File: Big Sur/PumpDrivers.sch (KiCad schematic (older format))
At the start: 3 parts, among them Q1 TSM900N10

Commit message: Work on pump drivers.
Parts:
- added D?: NTS12120EMFST1G, symbol Device:D_Schottky
- added Q?: TSM900N10, symbol Device:Q_NMOS_GDS
- added R?: 100K, symbol Device:R_US
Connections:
- net +24V: now also D?.1 (K)
- net GND: now also Q?.3 (S), R?.2
- new net PUMP_INPUT_2: Q?.1 (G), R?.1
- new net PUMP_LS_CHANNEL_2: D?.2 (A), Q?.2 (D)
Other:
- note removed: "Designing these to be low-side drivers cause why n-\nwait, why aren't we just using motor driver ICs for pumps\nlike we are for solenoids? They have safety features.\nAnd serial control. And blackjack. And hookers.\nOkay maybe not all of those, but still."
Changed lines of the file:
@@
 	1    0    0    -1
 $EndComp
-Text Notes 2650 2450 0    50   ~ 0
-Designing these to be low-side drivers cause why n-\nwait, why aren't we just using motor driver ICs for pumps\nlike we are for solenoids? They have safety features.\nAnd serial control. And blackjack. And hookers.\nOkay maybe not all of those, but still.
 Wire Wire Line
 	2500 1700 2500 1600
@@
 Text GLabel 1700 1900 0    50   BiDi ~ 0
 PUMP_INPUT_1
+$Comp
+L Device:Q_NMOS_GDS Q?
+U 1 1 5D85B099
+P 2400 3700
+F 0 "Q?" H 2606 3746 50  0000 L CNN
+F 1 "TSM900N10" H 2606 3655 50  0000 L CNN
+F 2 "" H 2600 3800 50  0001 C CNN
+F 3 "https://www.taiwansemi.com/products/datasheet/TSM900N10_A15.pdf" H 2400 3700 50  0001 C CNN
+F 4 "https://www.digikey.ca/product-detail/en/taiwan-semiconductor-corporation/TSM900N10CP-ROG/TSM900N10CPROGCT-ND/7360607" H 2400 3700 50  0001 C CNN "Digikey"
+	1    2400 3700
+	1    0    0    -1
+$EndComp
+Wire Wire Line
+	2500 3900 2500 4150
+$Comp
+L power:GND #PWR?
+U 1 1 5D85B0A4
+P 2500 4150
+F 0 "#PWR?" H 2500 3900 50  0001 C CNN
+F 1 "GND" H 2505 3977 50  0000 C CNN
+F 2 "" H 2500 4150 50  0001 C CNN
+F 3 "" H 2500 4150 50  0001 C CNN
+	1    2500 4150
+	1    0    0    -1
+$EndComp
+Wire Wire Line
+	2500 3500 2500 3400
+Wire Wire Line
+	2500 3400 2650 3400
+Text GLabel 2650 3400 2    50   BiDi ~ 0
+PUMP_LS_CHANNEL_2
+Connection ~ 2500 3400
+Wire Wire Line
+	2200 3700 2000 3700
+Wire Wire Line
+	2000 3700 2000 3750
+Connection ~ 2000 3700
+Wire Wire Line
+	2000 3700 1700 3700
+$Comp
+L Device:R_US R?
+U 1 1 5D85B0B6
+P 2000 3900
+F 0 "R?" H 2068 3946 50  0000 L CNN
+F 1 "100K" H 2068 3855 50  0000 L CNN
+F 2 "" V 2040 3890 50  0001 C CNN
+F 3 "~" H 2000 3900 50  0001 C CNN
+	1    2000 3900
+	1    0    0    -1
+$EndComp
+$Comp
+L power:GND #PWR?
+U 1 1 5D85B0C0
+P 2000 4150
+F 0 "#PWR?" H 2000 3900 50  0001 C CNN
+F 1 "GND" H 2005 3977 50  0000 C CNN
+F 2 "" H 2000 4150 50  0001 C CNN
+F 3 "" H 2000 4150 50  0001 C CNN
+	1    2000 4150
+	1    0    0    -1
+$EndComp
+Wire Wire Line
+	2000 4150 2000 4050
+Wire Wire Line
+	2500 3350 2500 3400
+$Comp
+L power:+24V #PWR?
+U 1 1 5D85B0CC
+P 2500 2950
+F 0 "#PWR?" H 2500 2800 50  0001 C CNN
+F 1 "+24V" H 2515 3123 50  0000 C CNN
+F 2 "" H 2500 2950 50  0001 C CNN
+F 3 "" H 2500 2950 50  0001 C CNN
+	1    2500 2950
+	1    0    0    -1
+$EndComp
+$Comp
+L Device:D_Schottky D?
+U 1 1 5D85B0D7
+P 2500 3200
+F 0 "D?" V 2454 3279 50  0000 L CNN
+F 1 "NTS12120EMFST1G" V 2545 3279 50  0000 L CNN
+F 2 "" H 2500 3200 50  0001 C CNN
+F 3 "https://www.onsemi.com/pub/Collateral/NTS12120EMFS-D.PDF" H 2500 3200 50  0001 C CNN
+F 4 "https://www.digikey.ca/product-detail/en/on-semiconductor/NTS12120EMFST1G/NTS12120EMFST1GOSCT-ND/8538813" V 2500 3200 50  0001 C CNN "Digikey"
+	1    2500 3200
+	0    1    1    0
+$EndComp
+Wire Wire Line
+	2500 2950 2500 3050
+Text GLabel 1700 3700 0    50   BiDi ~ 0
+PUMP_INPUT_2
 $EndSCHEMATC

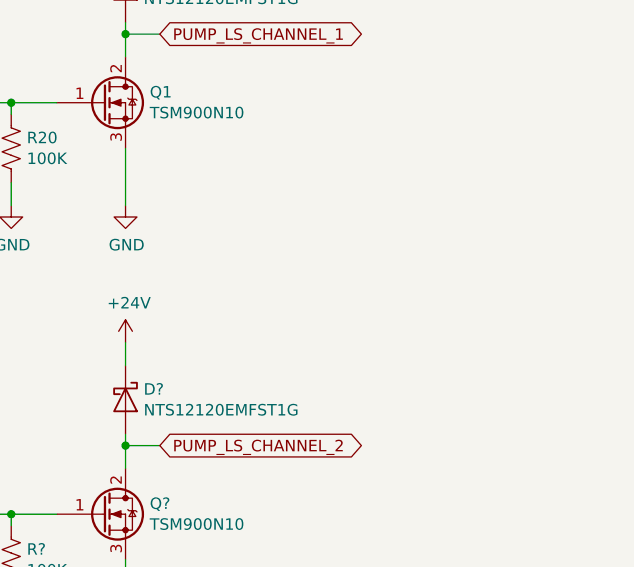
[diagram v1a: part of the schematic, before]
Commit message: Started filling in pinout of Paraduino connector, based on current Paraduino schematic.
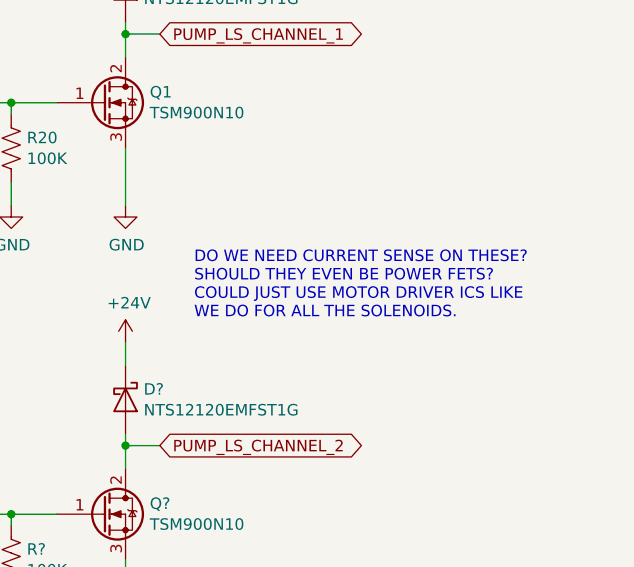
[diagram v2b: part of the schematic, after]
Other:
- note added: "DO WE NEED CURRENT SENSE ON THESE?\nSHOULD THEY EVEN BE POWER FETS?\nCOULD JUST USE MOTOR DRIVER ICS LIKE\nWE DO FOR ALL THE SOLENOIDS."
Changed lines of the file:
@@
 Text GLabel 1700 3700 0    50   BiDi ~ 0
 PUMP_INPUT_2
+Text Notes 2800 2850 0    50   ~ 0
+DO WE NEED CURRENT SENSE ON THESE?\nSHOULD THEY EVEN BE POWER FETS?\nCOULD JUST USE MOTOR DRIVER ICS LIKE\nWE DO FOR ALL THE SOLENOIDS.
 $EndSCHEMATC

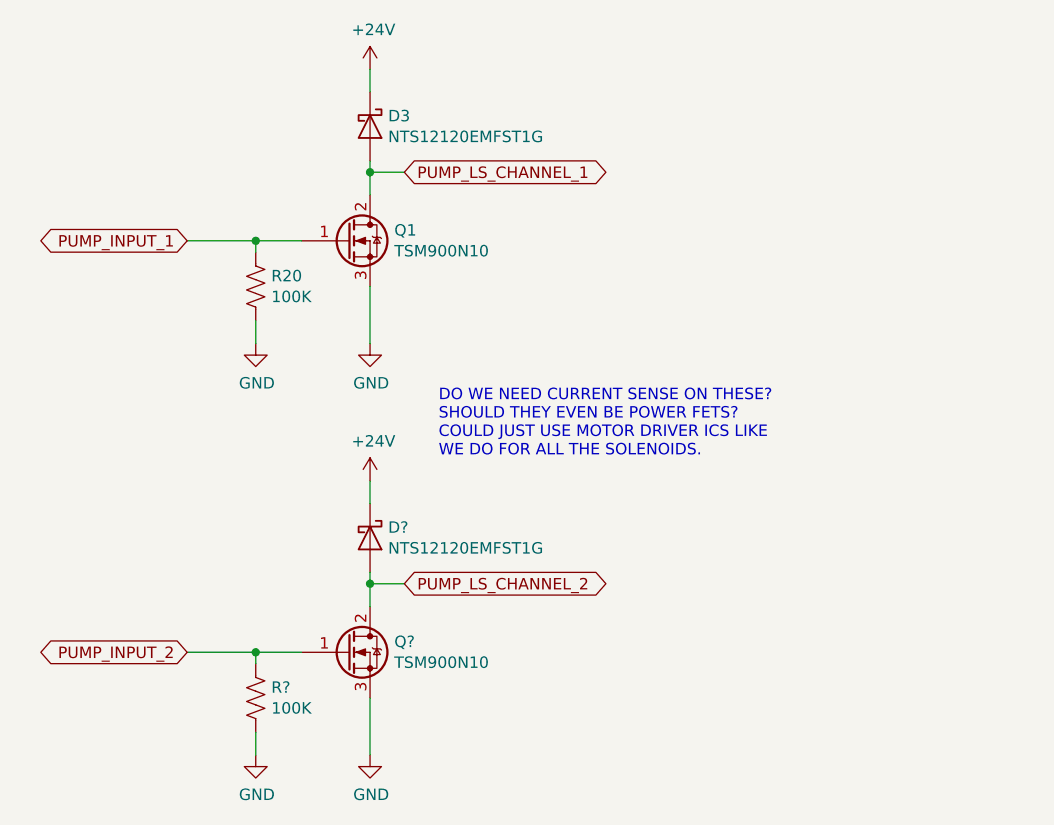
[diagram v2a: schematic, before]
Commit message: Updated current sense, second pump driver, solenoid connectors
-Current sense now uses current sense ICs, connected to Paraduino ADC pins.
-Added second pump driver.
-Connected outputs with XT30 connectors.
-Still need some Paraduino connections, inverter driver, footprints.
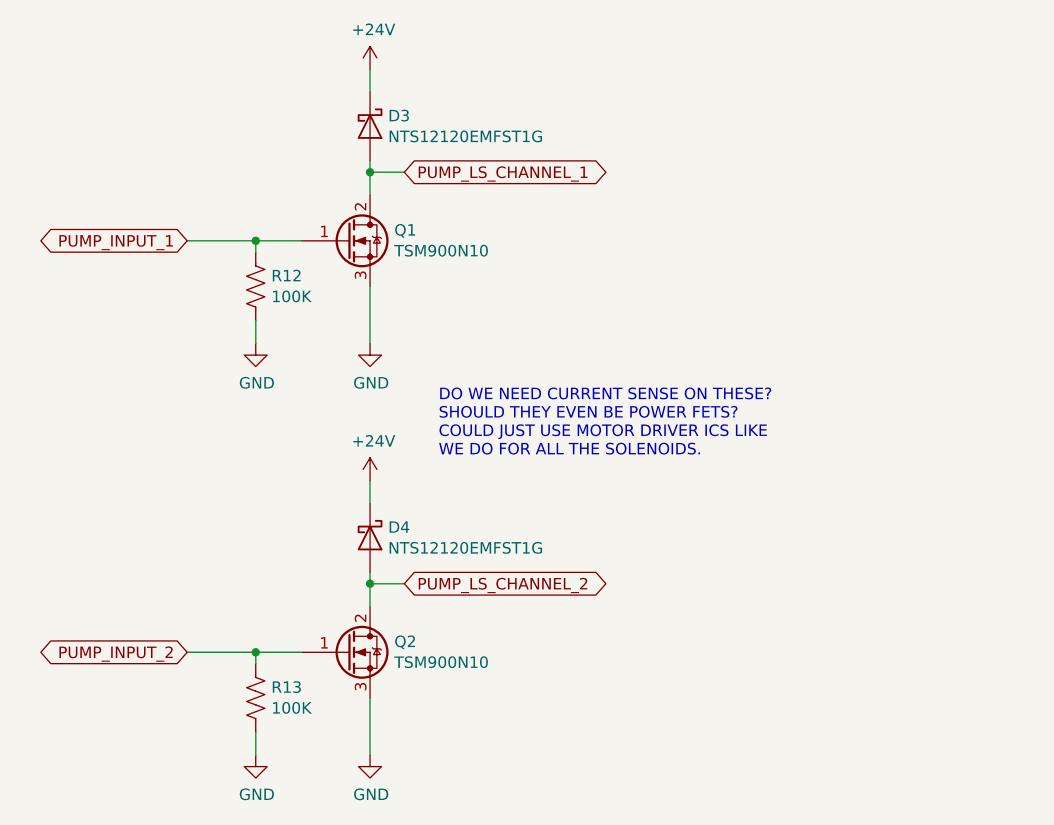
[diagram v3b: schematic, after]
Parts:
- gave numbers to parts that had none: 3
- renumbered R20 to R12
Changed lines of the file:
@@
 	2500 2100 2500 2350
 $Comp
-L power:GND #PWR033
+L power:GND #PWR038
 U 1 1 5D7D4C28
 P 2500 2350
-F 0 "#PWR033" H 2500 2100 50  0001 C CNN
+F 0 "#PWR038" H 2500 2100 50  0001 C CNN
 F 1 "GND" H 2505 2177 50  0000 C CNN
 F 2 "" H 2500 2350 50  0001 C CNN
@@
 	2000 1900 1700 1900
 $Comp
-L Device:R_US R20
+L Device:R_US R12
 U 1 1 5D7D75FE
 P 2000 2100
-F 0 "R20" H 2068 2146 50  0000 L CNN
+F 0 "R12" H 2068 2146 50  0000 L CNN
 F 1 "100K" H 2068 2055 50  0000 L CNN
 F 2 "" V 2040 2090 50  0001 C CNN
@@
 $EndComp
 $Comp
-L power:GND #PWR032
+L power:GND #PWR037
 U 1 1 5D7D85EE
 P 2000 2350
-F 0 "#PWR032" H 2000 2100 50  0001 C CNN
+F 0 "#PWR037" H 2000 2100 50  0001 C CNN
 F 1 "GND" H 2005 2177 50  0000 C CNN
 F 2 "" H 2000 2350 50  0001 C CNN
@@
 	2500 1550 2500 1600
 $Comp
-L power:+24V #PWR031
+L power:+24V #PWR036
 U 1 1 5D6DC51E
 P 2500 1150
-F 0 "#PWR031" H 2500 1000 50  0001 C CNN
+F 0 "#PWR036" H 2500 1000 50  0001 C CNN
 F 1 "+24V" H 2515 1323 50  0000 C CNN
 F 2 "" H 2500 1150 50  0001 C CNN
@@
 PUMP_INPUT_1
 $Comp
-L Device:Q_NMOS_GDS Q?
+L Device:Q_NMOS_GDS Q2
 U 1 1 5D85B099
 P 2400 3700
-F 0 "Q?" H 2606 3746 50  0000 L CNN
+F 0 "Q2" H 2606 3746 50  0000 L CNN
 F 1 "TSM900N10" H 2606 3655 50  0000 L CNN
 F 2 "" H 2600 3800 50  0001 C CNN
@@
 	2500 3900 2500 4150
 $Comp
-L power:GND #PWR?
+L power:GND #PWR041
 U 1 1 5D85B0A4
 P 2500 4150
-F 0 "#PWR?" H 2500 3900 50  0001 C CNN
+F 0 "#PWR041" H 2500 3900 50  0001 C CNN
 F 1 "GND" H 2505 3977 50  0000 C CNN
 F 2 "" H 2500 4150 50  0001 C CNN
@@
 	2000 3700 1700 3700
 $Comp
-L Device:R_US R?
+L Device:R_US R13
 U 1 1 5D85B0B6
 P 2000 3900
-F 0 "R?" H 2068 3946 50  0000 L CNN
+F 0 "R13" H 2068 3946 50  0000 L CNN
 F 1 "100K" H 2068 3855 50  0000 L CNN
 F 2 "" V 2040 3890 50  0001 C CNN
@@
 $EndComp
 $Comp
-L power:GND #PWR?
+L power:GND #PWR040
 U 1 1 5D85B0C0
 P 2000 4150
-F 0 "#PWR?" H 2000 3900 50  0001 C CNN
+F 0 "#PWR040" H 2000 3900 50  0001 C CNN
 F 1 "GND" H 2005 3977 50  0000 C CNN
 F 2 "" H 2000 4150 50  0001 C CNN
@@
 	2500 3350 2500 3400
 $Comp
-L power:+24V #PWR?
+L power:+24V #PWR039
 U 1 1 5D85B0CC
 P 2500 2950
-F 0 "#PWR?" H 2500 2800 50  0001 C CNN
+F 0 "#PWR039" H 2500 2800 50  0001 C CNN
 F 1 "+24V" H 2515 3123 50  0000 C CNN
 F 2 "" H 2500 2950 50  0001 C CNN
@@
 $EndComp
 $Comp
-L Device:D_Schottky D?
+L Device:D_Schottky D4
 U 1 1 5D85B0D7
 P 2500 3200
-F 0 "D?" V 2454 3279 50  0000 L CNN
+F 0 "D4" V 2454 3279 50  0000 L CNN
 F 1 "NTS12120EMFST1G" V 2545 3279 50  0000 L CNN
 F 2 "" H 2500 3200 50  0001 C CNN

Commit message: Removed Inverter
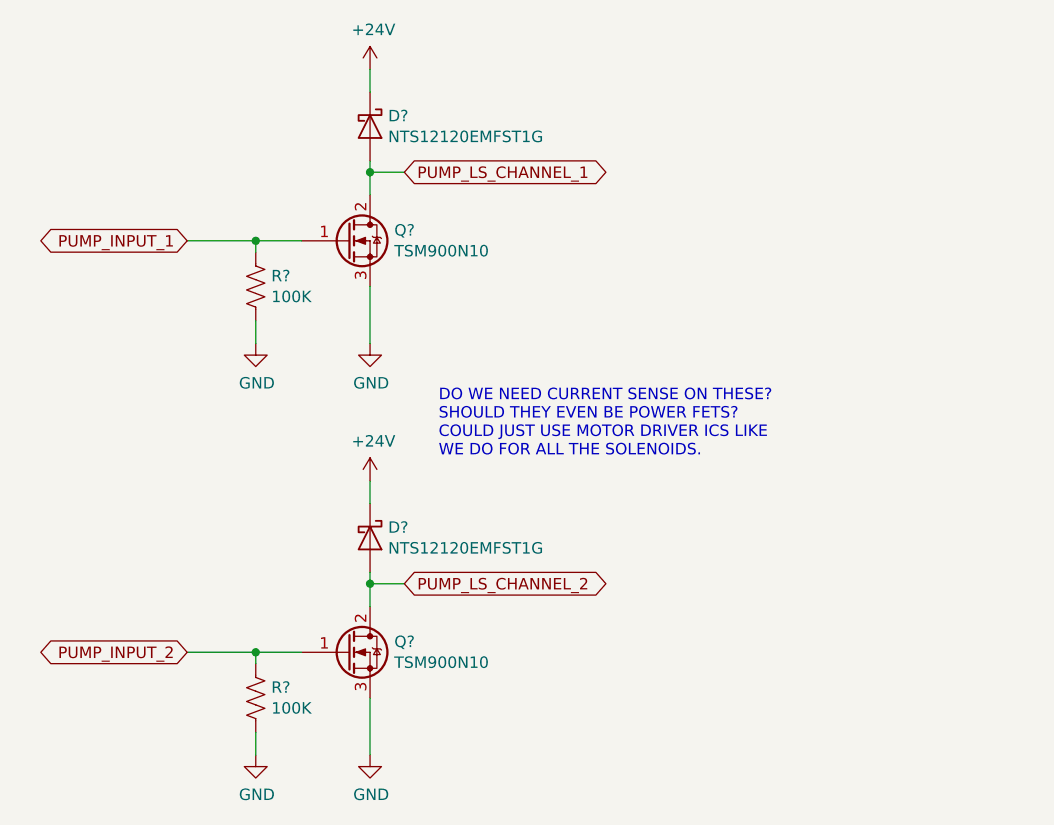
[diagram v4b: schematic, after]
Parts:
- renumbered D3 to D?, D4 to D?, Q1 to Q?, Q2 to Q?, R12 to R?, R13 to R?
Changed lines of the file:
@@
 $EndDescr
 $Comp
-L Device:Q_NMOS_GDS Q1
+L Device:Q_NMOS_GDS Q?
 U 1 1 5D7D3E10
 P 2400 1900
-F 0 "Q1" H 2606 1946 50  0000 L CNN
+F 0 "Q?" H 2606 1946 50  0000 L CNN
 F 1 "TSM900N10" H 2606 1855 50  0000 L CNN
 F 2 "" H 2600 2000 50  0001 C CNN
@@
 	2500 2100 2500 2350
 $Comp
-L power:GND #PWR038
+L power:GND #PWR?
 U 1 1 5D7D4C28
 P 2500 2350
-F 0 "#PWR038" H 2500 2100 50  0001 C CNN
+F 0 "#PWR?" H 2500 2100 50  0001 C CNN
 F 1 "GND" H 2505 2177 50  0000 C CNN
 F 2 "" H 2500 2350 50  0001 C CNN
@@
 	2000 1900 1700 1900
 $Comp
-L Device:R_US R12
+L Device:R_US R?
 U 1 1 5D7D75FE
 P 2000 2100
-F 0 "R12" H 2068 2146 50  0000 L CNN
+F 0 "R?" H 2068 2146 50  0000 L CNN
 F 1 "100K" H 2068 2055 50  0000 L CNN
 F 2 "" V 2040 2090 50  0001 C CNN
@@
 $EndComp
 $Comp
-L power:GND #PWR037
+L power:GND #PWR?
 U 1 1 5D7D85EE
 P 2000 2350
-F 0 "#PWR037" H 2000 2100 50  0001 C CNN
+F 0 "#PWR?" H 2000 2100 50  0001 C CNN
 F 1 "GND" H 2005 2177 50  0000 C CNN
 F 2 "" H 2000 2350 50  0001 C CNN
@@
 	2500 1550 2500 1600
 $Comp
-L power:+24V #PWR036
+L power:+24V #PWR?
 U 1 1 5D6DC51E
 P 2500 1150
-F 0 "#PWR036" H 2500 1000 50  0001 C CNN
+F 0 "#PWR?" H 2500 1000 50  0001 C CNN
 F 1 "+24V" H 2515 1323 50  0000 C CNN
 F 2 "" H 2500 1150 50  0001 C CNN
@@
 $EndComp
 $Comp
-L Device:D_Schottky D3
+L Device:D_Schottky D?
 U 1 1 5D6DD7E1
 P 2500 1400
-F 0 "D3" V 2454 1479 50  0000 L CNN
+F 0 "D?" V 2454 1479 50  0000 L CNN
 F 1 "NTS12120EMFST1G" V 2545 1479 50  0000 L CNN
 F 2 "" H 2500 1400 50  0001 C CNN
@@
 PUMP_INPUT_1
 $Comp
-L Device:Q_NMOS_GDS Q2
+L Device:Q_NMOS_GDS Q?
 U 1 1 5D85B099
 P 2400 3700
-F 0 "Q2" H 2606 3746 50  0000 L CNN
+F 0 "Q?" H 2606 3746 50  0000 L CNN
 F 1 "TSM900N10" H 2606 3655 50  0000 L CNN
 F 2 "" H 2600 3800 50  0001 C CNN
@@
 	2500 3900 2500 4150
 $Comp
-L power:GND #PWR041
+L power:GND #PWR?
 U 1 1 5D85B0A4
 P 2500 4150
-F 0 "#PWR041" H 2500 3900 50  0001 C CNN
+F 0 "#PWR?" H 2500 3900 50  0001 C CNN
 F 1 "GND" H 2505 3977 50  0000 C CNN
 F 2 "" H 2500 4150 50  0001 C CNN
@@
 	2000 3700 1700 3700
 $Comp
-L Device:R_US R13
+L Device:R_US R?
 U 1 1 5D85B0B6
 P 2000 3900
-F 0 "R13" H 2068 3946 50  0000 L CNN
+F 0 "R?" H 2068 3946 50  0000 L CNN
 F 1 "100K" H 2068 3855 50  0000 L CNN
 F 2 "" V 2040 3890 50  0001 C CNN
@@
 $EndComp
 $Comp
-L power:GND #PWR040
+L power:GND #PWR?
 U 1 1 5D85B0C0
 P 2000 4150
-F 0 "#PWR040" H 2000 3900 50  0001 C CNN
+F 0 "#PWR?" H 2000 3900 50  0001 C CNN
 F 1 "GND" H 2005 3977 50  0000 C CNN
 F 2 "" H 2000 4150 50  0001 C CNN
@@
 	2500 3350 2500 3400
 $Comp
-L power:+24V #PWR039
+L power:+24V #PWR?
 U 1 1 5D85B0CC
 P 2500 2950
-F 0 "#PWR039" H 2500 2800 50  0001 C CNN
+F 0 "#PWR?" H 2500 2800 50  0001 C CNN
 F 1 "+24V" H 2515 3123 50  0000 C CNN
 F 2 "" H 2500 2950 50  0001 C CNN
@@
 $EndComp
 $Comp
-L Device:D_Schottky D4
+L Device:D_Schottky D?
 U 1 1 5D85B0D7
 P 2500 3200
-F 0 "D4" V 2454 3279 50  0000 L CNN
+F 0 "D?" V 2454 3279 50  0000 L CNN
 F 1 "NTS12120EMFST1G" V 2545 3279 50  0000 L CNN
 F 2 "" H 2500 3200 50  0001 C CNN
